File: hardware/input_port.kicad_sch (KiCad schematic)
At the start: 25 parts, among them J401 10061913-102PLF, U301 TXB0108DQSR, U303 TXB0108DQSR, U305 TXB0108DQSR, U307 TXB0108DQSR, U309 TXB0108DQSR, U310 TXB0108DQSR, U311 TXB0108DQSR, U312 TXB0108DQSR

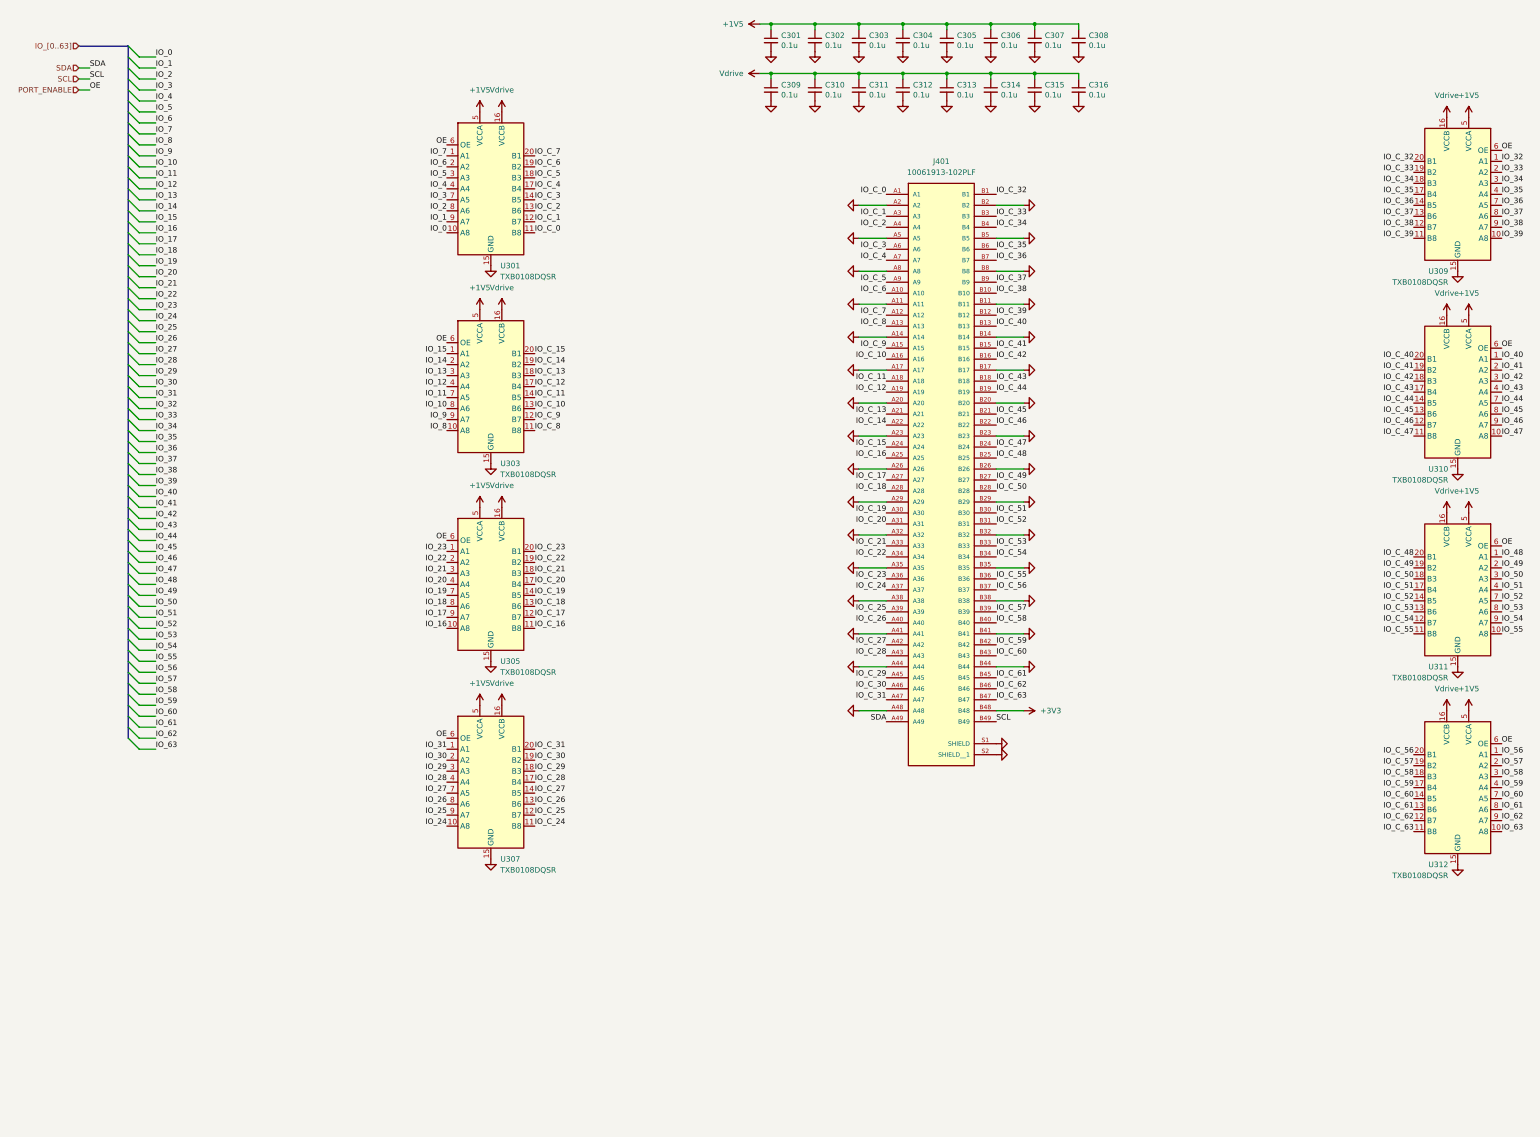
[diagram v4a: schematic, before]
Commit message: Moved to new level translator with less input current requirement
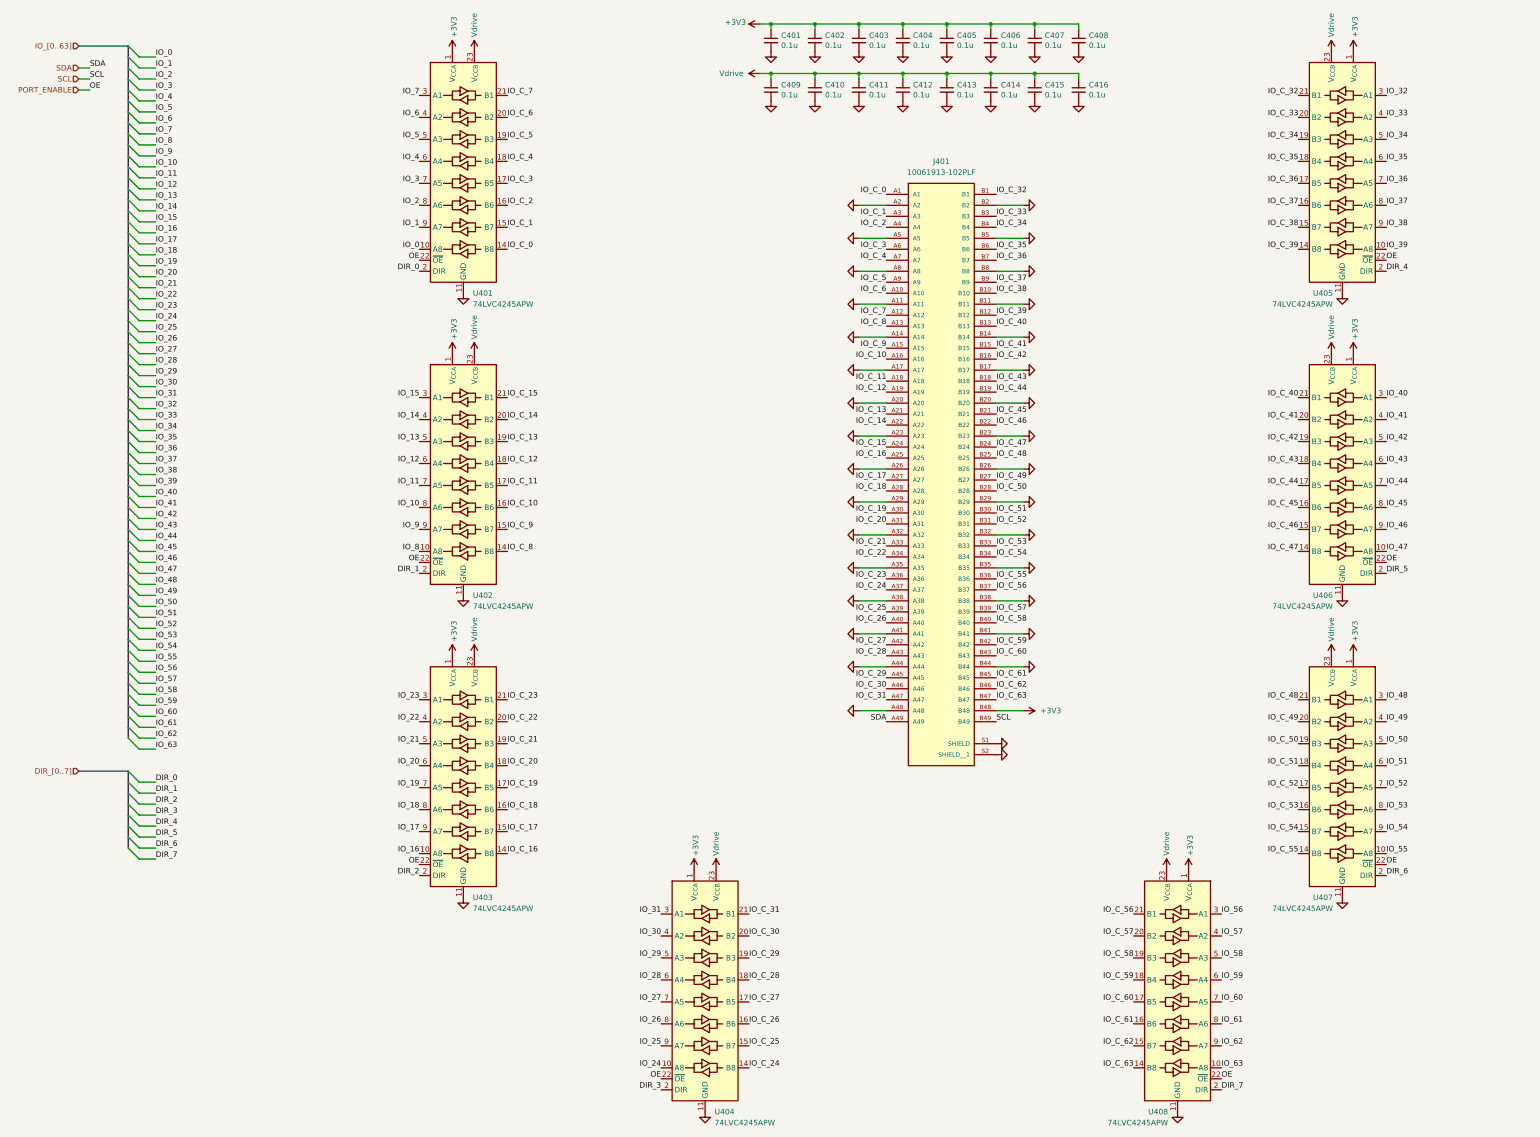
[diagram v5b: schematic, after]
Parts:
- removed U301, U303, U305, U307, U309, U310, U311, U312: TXB0108DQSR, Package_SON:USON-20_2x4mm_P0.4mm, symbol Logic_LevelTranslator:TXB0108DQSR
- added U401, U402, U403, U404, U405, U406, U407, U408: 74LVC4245APW, Package_SO:TSSOP-24_4.4x7.8mm_P0.65mm, symbol Logic_LevelTranslator:SN74LVC8T245
- C401: renamed from C301; footprint passive:C_0201 -> passive:C_0402
- C402: renamed from C302; footprint passive:C_0201 -> passive:C_0402
- C403: renamed from C303; footprint passive:C_0201 -> passive:C_0402
- C404: renamed from C304; footprint passive:C_0201 -> passive:C_0402
- C405: renamed from C305; footprint passive:C_0201 -> passive:C_0402
- C406: renamed from C306; footprint passive:C_0201 -> passive:C_0402
- C407: renamed from C307; footprint passive:C_0201 -> passive:C_0402
- C408: renamed from C308; footprint passive:C_0201 -> passive:C_0402
- C409: renamed from C309; footprint passive:C_0201 -> passive:C_0402
- C410: renamed from C310; footprint passive:C_0201 -> passive:C_0402
- C411: renamed from C311; footprint passive:C_0201 -> passive:C_0402
- C412: renamed from C312; footprint passive:C_0201 -> passive:C_0402
- C413: renamed from C313; footprint passive:C_0201 -> passive:C_0402
- C414: renamed from C314; footprint passive:C_0201 -> passive:C_0402
- C415: renamed from C315; footprint passive:C_0201 -> passive:C_0402
- C416: renamed from C316; footprint passive:C_0201 -> passive:C_0402
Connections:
- net +1V5 is gone; now on net +3V3: C401.1, C402.1, C403.1, C404.1, C405.1, C406.1, C407.1, C408.1
- net +3V3: now also U401.1 (V_{CCA}), U402.1 (V_{CCA}), U403.1 (V_{CCA}), U404.1 (V_{CCA}), U405.1 (V_{CCA}), U406.1 (V_{CCA}), U407.1 (V_{CCA}), U408.1 (V_{CCA})
- net GND: now also U401.11 (GND), U401.12 (GND), U401.13 (GND), U402.11 (GND), U402.12 (GND), U402.13 (GND), U403.11 (GND), U403.12 (GND), U403.13 (GND), U404.11 (GND), U404.12 (GND), U404.13 (GND), U405.11 (GND), U405.12 (GND), U405.13 (GND), U406.11 (GND), U406.12 (GND), U406.13 (GND), U407.11 (GND), U407.12 (GND), U407.13 (GND), U408.11 (GND), U408.12 (GND), U408.13 (GND)
- net IO_0: now also U401.10 (A8)
- net IO_1: now also U401.9 (A7)
- net IO_10: now also U402.8 (A6)
- net IO_11: now also U402.7 (A5)
- net IO_12: now also U402.6 (A4)
- net IO_13: now also U402.5 (A3)
- net IO_14: now also U402.4 (A2)
- net IO_15: now also U402.3 (A1)
- net IO_16: now also U403.10 (A8)
- net IO_17: now also U403.9 (A7)
- net IO_18: now also U403.8 (A6)
- net IO_19: now also U403.7 (A5)
- net IO_2: now also U401.8 (A6)
- net IO_20: now also U403.6 (A4)
- net IO_21: now also U403.5 (A3)
- net IO_22: now also U403.4 (A2)
- net IO_23: now also U403.3 (A1)
- net IO_24: now also U404.10 (A8)
- net IO_25: now also U404.9 (A7)
- net IO_26: now also U404.8 (A6)
- net IO_27: now also U404.7 (A5)
- net IO_28: now also U404.6 (A4)
- net IO_29: now also U404.5 (A3)
- net IO_3: now also U401.7 (A5)
- net IO_30: now also U404.4 (A2)
- net IO_31: now also U404.3 (A1)
- net IO_32: now also U405.3 (A1)
- net IO_33: now also U405.4 (A2)
- net IO_34: now also U405.5 (A3)
- net IO_35: now also U405.6 (A4)
- net IO_36: now also U405.7 (A5)
- net IO_37: now also U405.8 (A6)
- net IO_38: now also U405.9 (A7)
- net IO_39: now also U405.10 (A8)
- net IO_4: now also U401.6 (A4)
- net IO_40: now also U406.3 (A1)
- net IO_41: now also U406.4 (A2)
- net IO_42: now also U406.5 (A3)
- net IO_43: now also U406.6 (A4)
- net IO_44: now also U406.7 (A5)
- net IO_45: now also U406.8 (A6)
- net IO_46: now also U406.9 (A7)
- net IO_47: now also U406.10 (A8)
- net IO_48: now also U407.3 (A1)
- net IO_49: now also U407.4 (A2)
- net IO_5: now also U401.5 (A3)
- net IO_50: now also U407.5 (A3)
- net IO_51: now also U407.6 (A4)
- net IO_52: now also U407.7 (A5)
- net IO_53: now also U407.8 (A6)
- net IO_54: now also U407.9 (A7)
- net IO_55: now also U407.10 (A8)
- net IO_56: now also U408.3 (A1)
- net IO_57: now also U408.4 (A2)
- net IO_58: now also U408.5 (A3)
- net IO_59: now also U408.6 (A4)
- net IO_6: now also U401.4 (A2)
- net IO_60: now also U408.7 (A5)
- net IO_61: now also U408.8 (A6)
- net IO_62: now also U408.9 (A7)
- net IO_63: now also U408.10 (A8)
- net IO_7: now also U401.3 (A1)
- net IO_8: now also U402.10 (A8)
- net IO_9: now also U402.9 (A7)
- net IO_C_0: now also U401.14 (B8)
- net IO_C_1: now also U401.15 (B7)
- net IO_C_10: now also U402.16 (B6)
- net IO_C_11: now also U402.17 (B5)
- net IO_C_12: now also U402.18 (B4)
- net IO_C_13: now also U402.19 (B3)
- net IO_C_14: now also U402.20 (B2)
- net IO_C_15: now also U402.21 (B1)
- net IO_C_16: now also U403.14 (B8)
- net IO_C_17: now also U403.15 (B7)
- net IO_C_18: now also U403.16 (B6)
- net IO_C_19: now also U403.17 (B5)
- net IO_C_2: now also U401.16 (B6)
- net IO_C_20: now also U403.18 (B4)
- net IO_C_21: now also U403.19 (B3)
- net IO_C_22: now also U403.20 (B2)
- net IO_C_23: now also U403.21 (B1)
- net IO_C_24: now also U404.14 (B8)
- net IO_C_25: now also U404.15 (B7)
- net IO_C_26: now also U404.16 (B6)
- net IO_C_27: now also U404.17 (B5)
- net IO_C_28: now also U404.18 (B4)
- net IO_C_29: now also U404.19 (B3)
- net IO_C_3: now also U401.17 (B5)
- net IO_C_30: now also U404.20 (B2)
- net IO_C_31: now also U404.21 (B1)
- net IO_C_32: now also U405.21 (B1)
- net IO_C_33: now also U405.20 (B2)
- net IO_C_34: now also U405.19 (B3)
- net IO_C_35: now also U405.18 (B4)
- net IO_C_36: now also U405.17 (B5)
- net IO_C_37: now also U405.16 (B6)
- net IO_C_38: now also U405.15 (B7)
- net IO_C_39: now also U405.14 (B8)
- net IO_C_4: now also U401.18 (B4)
- net IO_C_40: now also U406.21 (B1)
- net IO_C_41: now also U406.20 (B2)
- net IO_C_42: now also U406.19 (B3)
- net IO_C_43: now also U406.18 (B4)
- net IO_C_44: now also U406.17 (B5)
- net IO_C_45: now also U406.16 (B6)
- net IO_C_46: now also U406.15 (B7)
- net IO_C_47: now also U406.14 (B8)
- net IO_C_48: now also U407.21 (B1)
- net IO_C_49: now also U407.20 (B2)
- net IO_C_5: now also U401.19 (B3)
- net IO_C_50: now also U407.19 (B3)
- net IO_C_51: now also U407.18 (B4)
- net IO_C_52: now also U407.17 (B5)
- net IO_C_53: now also U407.16 (B6)
- net IO_C_54: now also U407.15 (B7)
- net IO_C_55: now also U407.14 (B8)
- net IO_C_56: now also U408.21 (B1)
- net IO_C_57: now also U408.20 (B2)
- net IO_C_58: now also U408.19 (B3)
- net IO_C_59: now also U408.18 (B4)
- net IO_C_6: now also U401.20 (B2)
- net IO_C_60: now also U408.17 (B5)
- net IO_C_61: now also U408.16 (B6)
- net IO_C_62: now also U408.15 (B7)
- net IO_C_63: now also U408.14 (B8)
- net IO_C_7: now also U401.21 (B1)
- net IO_C_8: now also U402.14 (B8)
- net IO_C_9: now also U402.15 (B7)
- net PORT_ENABLE: now also U401.22 (~{OE}), U402.22 (~{OE}), U403.22 (~{OE}), U404.22 (~{OE}), U405.22 (~{OE}), U406.22 (~{OE}), U407.22 (~{OE}), U408.22 (~{OE})
- net Vdrive: now also U401.23 (V_{CCB}), U401.24 (V_{CCB}), U402.23 (V_{CCB}), U402.24 (V_{CCB}), U403.23 (V_{CCB}), U403.24 (V_{CCB}), U404.23 (V_{CCB}), U404.24 (V_{CCB}), U405.23 (V_{CCB}), U405.24 (V_{CCB}), U406.23 (V_{CCB}), U406.24 (V_{CCB}), U407.23 (V_{CCB}), U407.24 (V_{CCB}), U408.23 (V_{CCB}), U408.24 (V_{CCB})
- new net DIR_0: U401.2 (DIR)
- new net DIR_1: U402.2 (DIR)
- new net DIR_2: U403.2 (DIR)
- new net DIR_3: U404.2 (DIR)
- new net DIR_4: U405.2 (DIR)
- new net DIR_5: U406.2 (DIR)
- new net DIR_6: U407.2 (DIR)
- new net DIR_7: U408.2 (DIR)
